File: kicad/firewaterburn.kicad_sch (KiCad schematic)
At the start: 5 parts, among them P1 USB_C_Plug_USB2.0

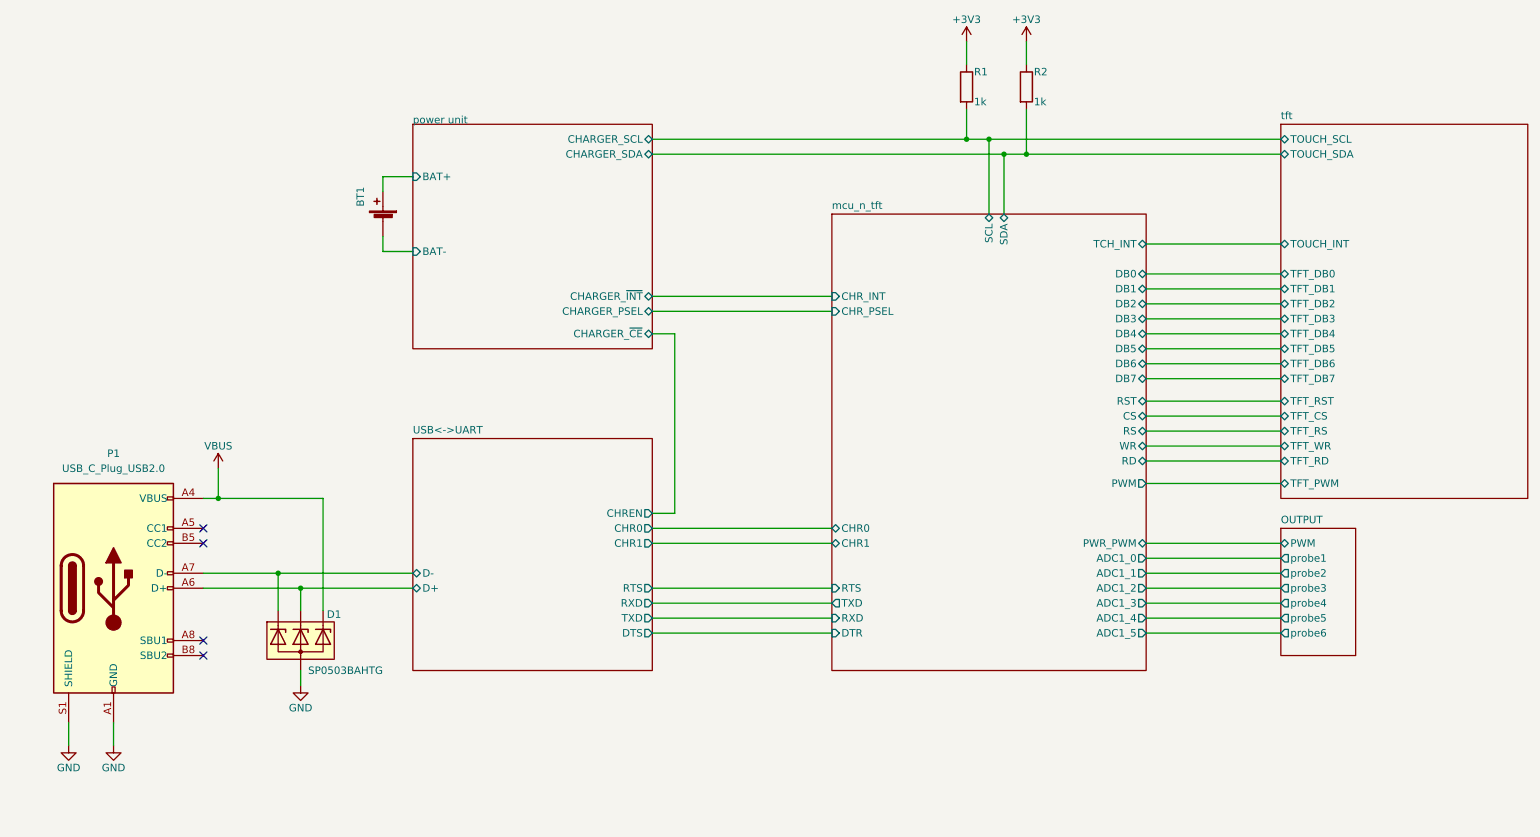
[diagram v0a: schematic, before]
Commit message: refactor KiCAD Project to v6
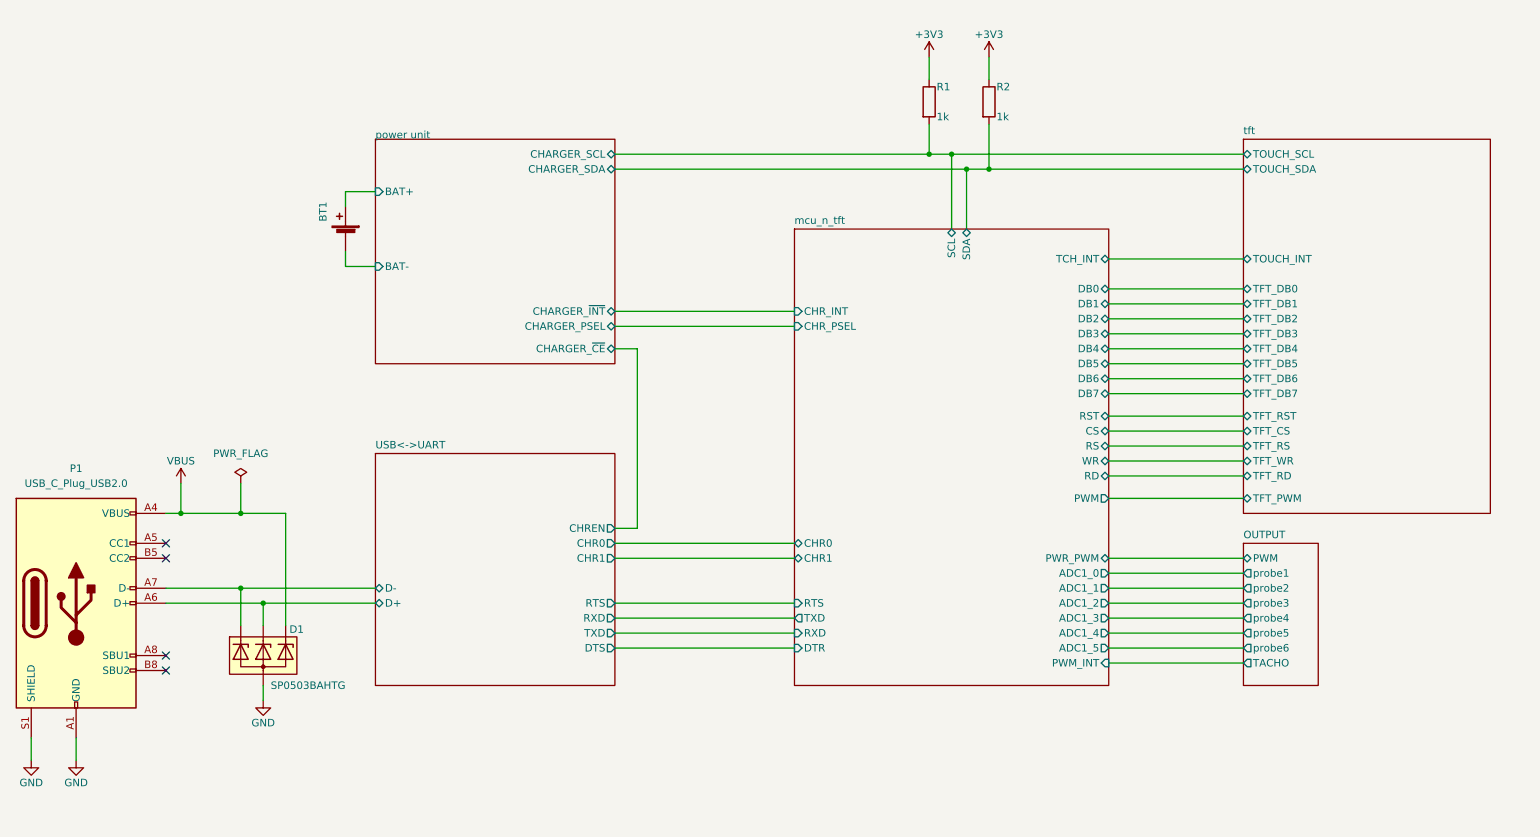
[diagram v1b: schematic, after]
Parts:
- BT1: Digikey (none) -> -
- D1: Digikey (none) -> F2715CT-ND
- R1, R2: Digikey (none) -> A129688CT-ND
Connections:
- net USB<->UART/D+: now also D1.3 (K); no longer D1.2 (K)
- net VBUS: now also D1.4 (K); no longer D1.2 (K)
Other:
- sheet OUTPUT ports: added TACHO; removed none
- sheet mcu_n_tft ports: added PWM_INT; removed none

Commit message: add connection to lcd
import parts into pcbnew
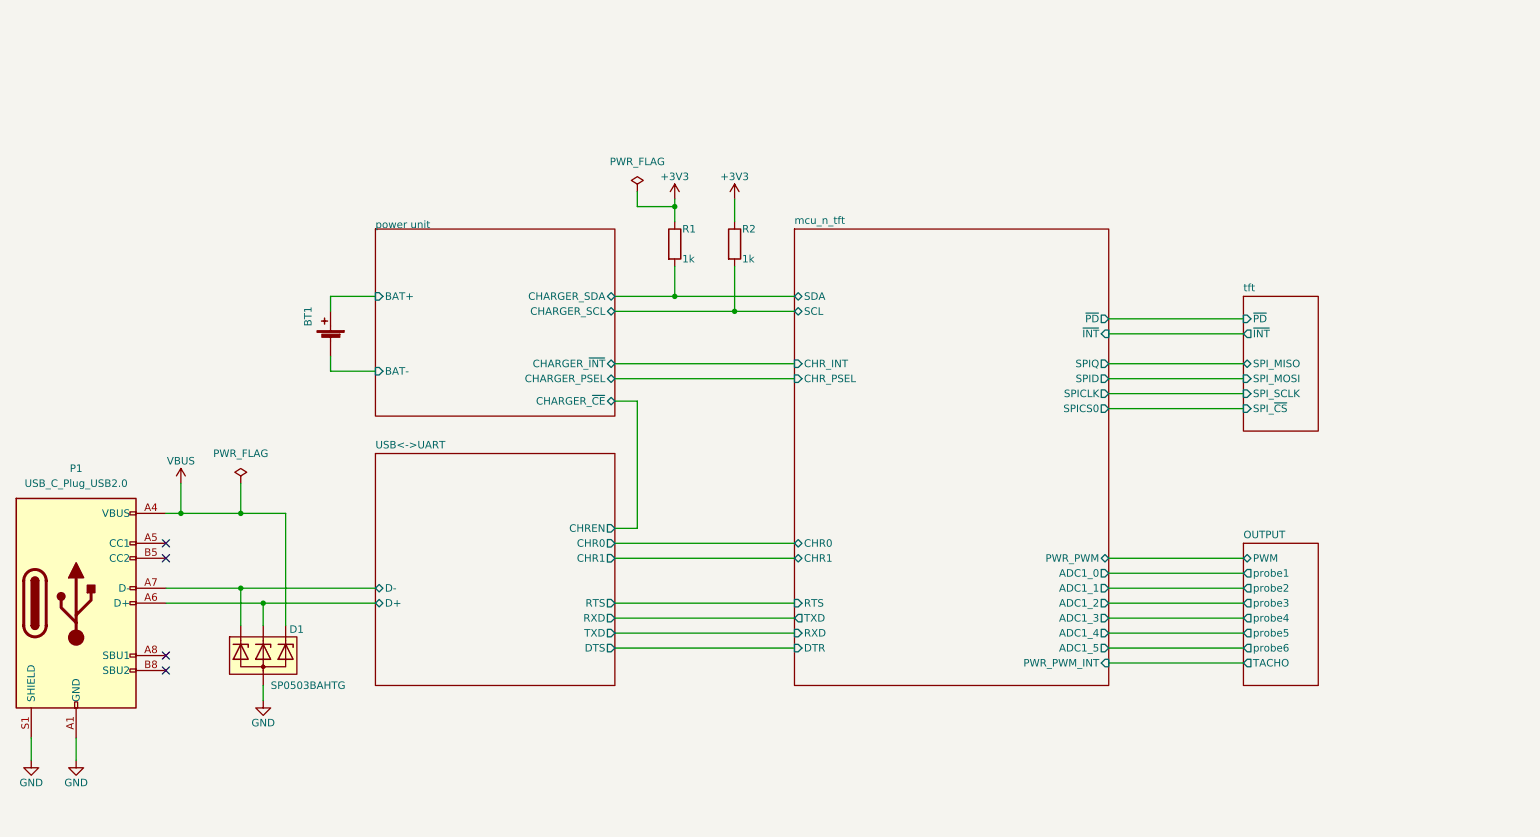
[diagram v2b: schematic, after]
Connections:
- net GND: now also P1.1 (GND), P1.2 (GND)
- net mcu_n_tft/SCL: now also R2.2; no longer R1.2
- net mcu_n_tft/SDA: now also R1.2; no longer R2.2
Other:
- sheet mcu_n_tft ports: added PWR_PWM_INT, SPICLK, SPICS0, SPID, SPIQ, ~{INT}, ~{PD}; removed CS, DB0, DB1, DB2, DB3, DB4, DB5, DB6, DB7, PWM, PWM_INT, RD, RS, RST, TCH_INT, WR
- sheet tft ports: added SPI_MISO, SPI_MOSI, SPI_SCLK, SPI_~{CS}, ~{INT}, ~{PD}; removed TFT_CS, TFT_DB0, TFT_DB1, TFT_DB2, TFT_DB3, TFT_DB4, TFT_DB5, TFT_DB6, TFT_DB7, TFT_PWM, TFT_RD, TFT_RS, TFT_RST, TFT_WR, TOUCH_INT, TOUCH_SCL, TOUCH_SDA
- moved on the sheet: BT1, R1, R2

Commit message: rework pcb
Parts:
- removed BT1: Battery_Cell, Connector_JST:JST_PH_S2B-PH-K_1x02_P2.00mm_Horizontal, symbol Device:Battery_Cell
- D1: symbol z_ic:SP0503BAHTG -> mylib_ic:SP0503BAHTG
- P1: footprint z_connector:USB_C_Receptacle_Amphenol_12401548E4-2A -> mylib_connector:USB_C_Receptacle_Amphenol_12401548E4-2A; symbol z_connectors:USB_C_Plug_USB2.0 -> mylib_connectors:USB_C_Plug_USB2.0
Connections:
- net USB<->UART/D+ renamed mcu_n_tft/D+
- net USB<->UART/D- renamed mcu_n_tft/D-
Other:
- removed sheet USB<->UART
- removed sheet power unit
- added sheet pwr_supply (pwr_supply.kicad_sch)
- sheet mcu_n_tft ports: added ADC_0, ADC_1, ADC_2, ADC_3, ADC_4, ADC_5, D+, D-, QSPI_CLK, QSPI_IO0, QSPI_IO1, QSPI_IO2, QSPI_IO3, QSPI_~{CS}; removed ADC1_0, ADC1_1, ADC1_2, ADC1_3, ADC1_4, ADC1_5, CHR0, CHR1, CHR_INT, CHR_PSEL, DTR, RTS, RXD, SPICLK, SPICS0, SPID, SPIQ, TXD
- sheet tft ports: added GPIO0.0, QSPI_IO.0, QSPI_IO.1, QSPI_IO.2, QSPI_IO.3, QSPI_SCLK, QSPI_~{CS}; removed SPI_MISO, SPI_MOSI, SPI_SCLK, SPI_~{CS}

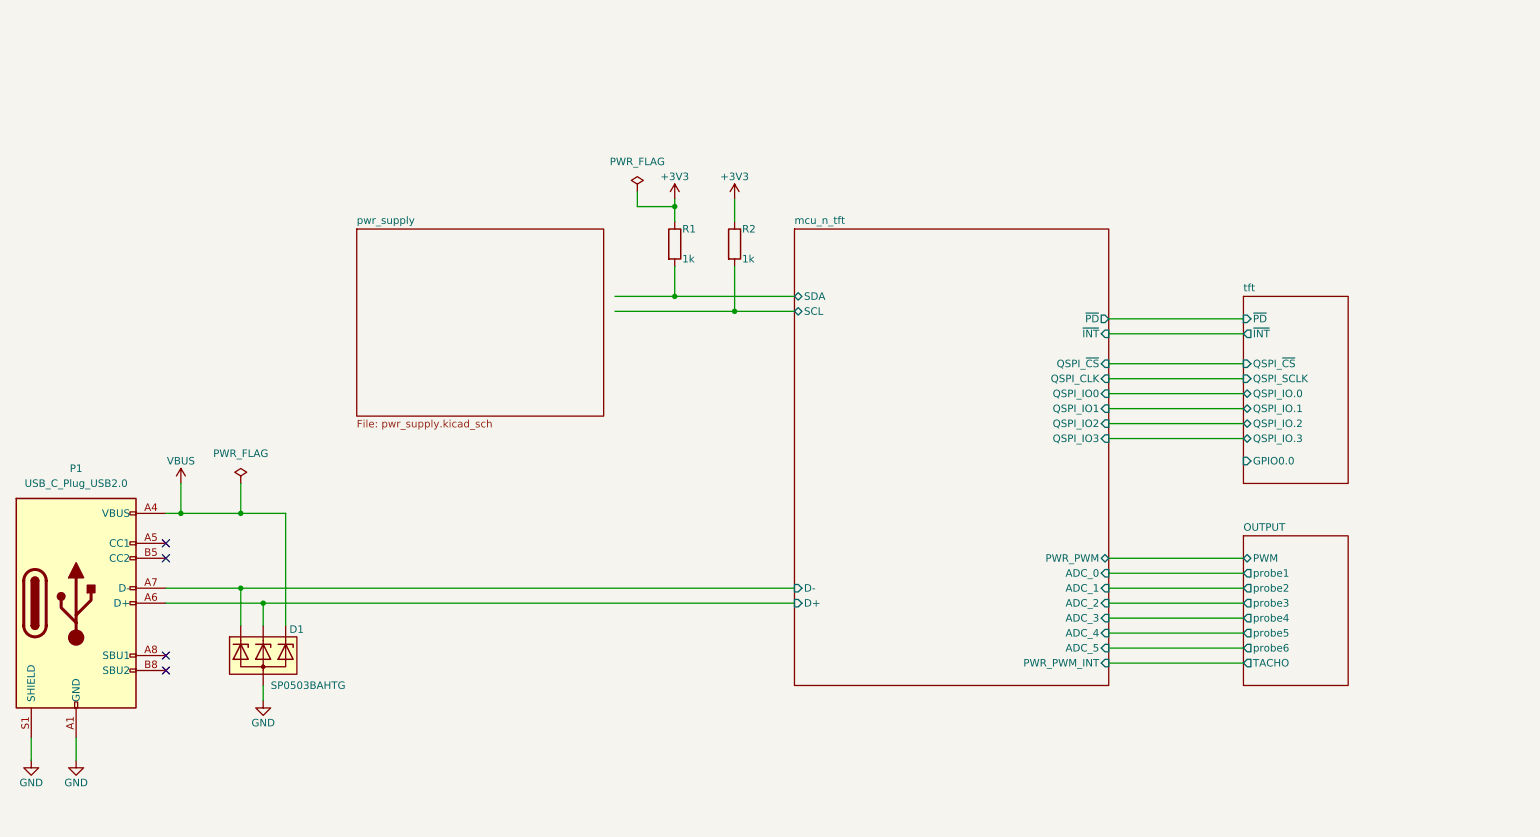
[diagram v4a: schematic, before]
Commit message: add all digikeys numbers to schematic
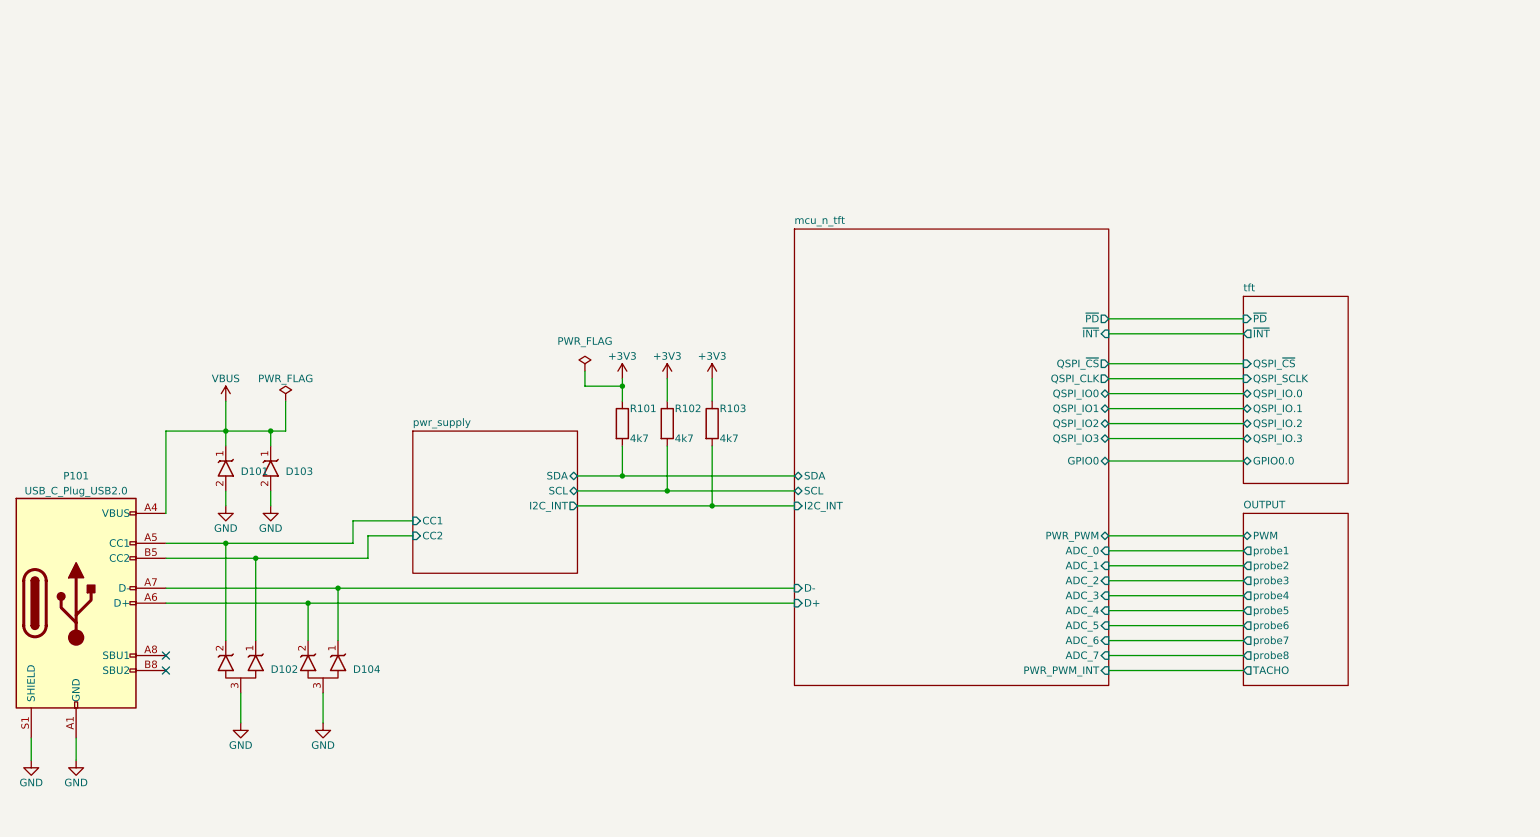
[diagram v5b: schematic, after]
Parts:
- removed D1: SP0503BAHTG, Package_TO_SOT_SMD:SOT-143, symbol mylib_ic:SP0503BAHTG
- removed P1: USB_C_Plug_USB2.0, mylib_connector:USB_C_Receptacle_Amphenol_12401548E4-2A, symbol mylib_connectors:USB_C_Plug_USB2.0
- added D101, D103: ESDA25P35, mylib_ic:D_0604_1610Metric, symbol mylib_ic:ESDA25P35
- added D102, D104: ESDA25W, Package_TO_SOT_SMD:SOT-323_SC-70, symbol mylib_ic:ESDA25W
- added P101: USB_C_Plug_USB2.0, mylib_connector:USB_C_Receptacle_Molex_C_24P_SMD_RA, symbol mylib_connectors:USB_C_Plug_USB2.0
- added R103: 4k7, Resistor_SMD:R_0603_1608Metric, symbol Device:R
- R101: renamed from R1; value 1k -> 4k7; Digikey A129688CT-ND -> 311-4.70KHRCT-ND
- R102: renamed from R2; value 1k -> 4k7; Digikey A129688CT-ND -> 311-4.70KHRCT-ND
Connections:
- net +3V3: now also R103.1
- net GND: now also D101.2, D102.3, D103.2, D104.3, P101.A1 (GND), P101.A12 (GND), P101.B1 (GND), P101.B12 (GND), P101.S1 (SHIELD)
- net VBUS: now also D101.1, D103.1, P101.A4 (VBUS), P101.A9 (VBUS), P101.B4 (VBUS), P101.B9 (VBUS)
- net mcu_n_tft/D+: now also D104.2, P101.A6 (D+), P101.B6 (D+)
- net mcu_n_tft/D-: now also D104.1, P101.A7 (D-), P101.B7 (D-)
- new net mcu_n_tft/I2C_INT: R103.2
- new net pwr_supply/CC1: D102.2, P101.A5 (CC1)
- new net pwr_supply/CC2: D102.1, P101.B5 (CC2)
- no-connect marks 4 -> 2
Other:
- sheet OUTPUT ports: added probe7, probe8; removed none
- sheet mcu_n_tft ports: added ADC_6, ADC_7, GPIO0, I2C_INT; removed none
- sheet pwr_supply ports: added CC1, CC2, I2C_INT, SCL, SDA; removed none
- moved on the sheet: R101, R102

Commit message: wip
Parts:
- removed D102, D104: ESDA25W, Package_TO_SOT_SMD:SOT-323_SC-70, symbol mylib_ic:ESDA25W
- added U101: TPD4E02B04DQA, Package_SON:USON-10_2.5x1.0mm_P0.5mm, symbol Power_Protection:TPD4E02B04DQA
- renumbered D103 to D102
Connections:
- net GND: now also U101.3 (G), U101.8 (G)
- net pwr_supply/CC1: now also U101.1 (IO1), U101.10 (NC)
- net pwr_supply/CC2: now also U101.2 (IO2), U101.9 (NC)
- net mcu_n_tft/D+ renamed D+
- net D+: now also U101.5 (IO4), U101.6 (NC)
- net mcu_n_tft/D- renamed D-
- net D-: now also U101.4 (IO3), U101.7 (NC)
